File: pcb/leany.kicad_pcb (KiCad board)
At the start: 2 copper layers, 89.4 x 69 mm, 73 parts, among them J1 ST7735S, J2 SWD, J3 USB C, J4 BATT, Q1 AO3401A, Q2 AO3400A, Q3 AO3401A, SW1 ZERO, SW2 HOLD, SW3 RESET, SW4 FLASH, SW5 POWER, U1 STM32F103C8Tx, U2 CH340C, U3 BMI270, U4 BQ25619, U5 AP2112K-3.3, Y1 8MHz

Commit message: refactor: replace the LSM6DSO by a BMI270 (#5)
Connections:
- net /LSM6DSO_CS renamed /BMI270_CS
- net /LSM6DSO_INT1 renamed /BMI270_INT1
- net /LSM6DSO_INT2 renamed /BMI270_INT2
- net /LSM6DSO_SCL renamed /BMI270_SCL
- net /LSM6DSO_SDA renamed /BMI270_SDA
- net /LSM6DSO_SDO renamed /BMI270_SDO

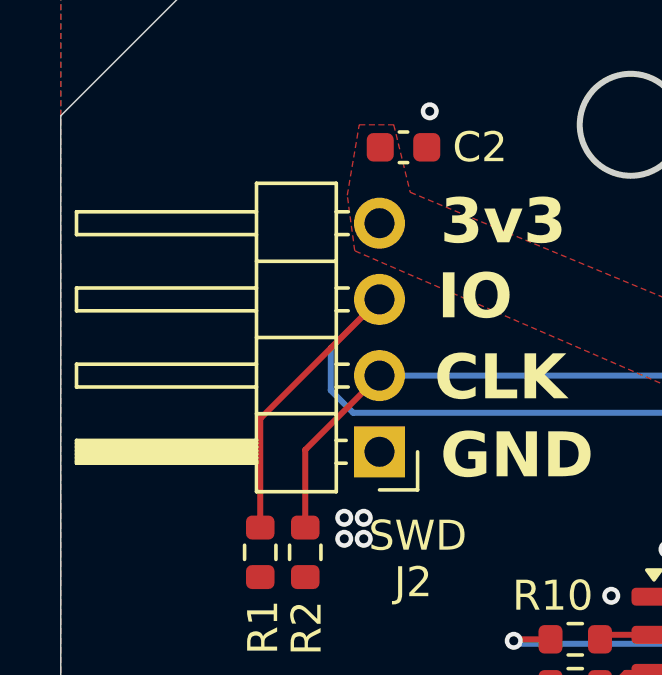
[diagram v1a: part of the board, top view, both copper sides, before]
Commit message: perf: strenghen Mahony filter (#50)
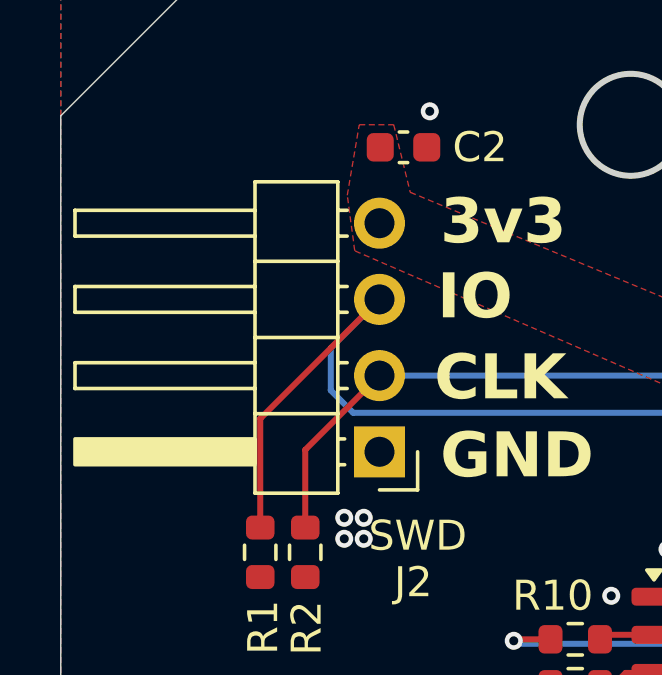
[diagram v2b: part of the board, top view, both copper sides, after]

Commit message: feat: design PCB rev0.3 (#27)
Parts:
- added C25: 100n, leany_footprints:C_0402_1005Metric, F.Cu at (164.9, 103.5)
- added C26: 100n, leany_footprints:C_0402_1005Metric, F.Cu at (149.4, 102.3)
- added C28: 100n, leany_footprints:C_0402_1005Metric, F.Cu at (136.5, 113.2)
- added Q4: AO3401A, Package_TO_SOT_SMD:SOT-23, F.Cu at (130.3, 110.5)
- added Q5: PT8810, Package_TO_SOT_SMD:SOT-23-6, F.Cu at (146.5, 112.6)
- added R25: 100R, leany_footprints:R_0402_1005Metric, F.Cu at (136.5, 111.3)
- added R26: 1k, leany_footprints:R_0402_1005Metric, F.Cu at (142.9, 112.7)
- added REF**: MountingHole_3mm, MountingHole:MountingHole_3mm, F.Cu at (119.6, 121.8)
- added REF**: MountingHole_3mm, MountingHole:MountingHole_3mm, F.Cu at (181.5, 87.0)
- added REF**: MountingHole_3mm, MountingHole:MountingHole_3mm, F.Cu at (181.5, 120.1)
- added TP6: Vin, leany_footprints:TestPoint_Pad_1.0x1.0mm, F.Cu at (137.2, 102.0)
- added TP7: 3.3V, leany_footprints:TestPoint_Pad_1.0x1.0mm, F.Cu at (139.7, 102.0)
- added U6: DW01A, Package_TO_SOT_SMD:SOT-23-6, F.Cu at (139.5, 112.7)
- C10, C12, C14, C17, C2, C20, C21, C22, C23, C3, C4, C5, C6, C7, C8, C9: footprint Capacitor_SMD:C_0603_1608Metric -> leany_footprints:C_0402_1005Metric
- J3: footprint Connector_USB:USB_C_Receptacle_HRO_TYPE-C-31-M-12 -> leany_footprints:USB_C_Receptacle_HRO_TYPE-C-31-M-12
- J4: footprint leany_footprints:wago_2060-452_998-404 -> leany_footprints:wago_2059-302_998-403
- R1, R11, R13, R14, R15, R16, R17, R18, R19, R2, R20, R23, R24, R3, R8: footprint Resistor_SMD:R_0603_1608Metric -> leany_footprints:R_0402_1005Metric
- R10: value 4k7 -> 10k; footprint Resistor_SMD:R_0603_1608Metric -> leany_footprints:R_0402_1005Metric
- R12: value 10k -> 4k7; footprint Resistor_SMD:R_0603_1608Metric -> leany_footprints:R_0402_1005Metric
- R7: value 1M -> 10k; footprint Resistor_SMD:R_0603_1608Metric -> leany_footprints:R_0402_1005Metric
- R9: value 10k -> 1M; footprint Resistor_SMD:R_0603_1608Metric -> leany_footprints:R_0402_1005Metric
- SW1: value ZERO -> SW_HIGH
- SW2: value HOLD -> SW_HIGH
- SW3: value RESET -> SW_LOW; footprint Button_Switch_SMD:SW_Push_1P1T_XKB_TS-1187A -> leany_footprints:SW_Push_1P1T_XKB_TS-1187A
- SW4: value FLASH -> SW_LOW; footprint Button_Switch_SMD:SW_Push_1P1T_XKB_TS-1187A -> leany_footprints:SW_Push_1P1T_XKB_TS-1187A
- TP1: value GND -> DEBUG_OUT
- TP2: value VBUS -> GND
- TP3: value BATT -> VBUS
- TP4: value Vin -> BATT
- TP5: value 3.3V -> +BATT
- U2: value CH340C -> CH340N; footprint Package_SO:SOIC-16_3.9x9.9mm_P1.27mm -> leany_footprints:SOP-8_3.9x4.9mm_P1.27mm
- U3: value BMI270 -> ICM-42688-P
- U5: footprint leany_footprints:TSOT-23-5 -> Package_TO_SOT_SMD:SOT-23-5
- moved TP1 68.7 mm to (163.6, 82.8)
- moved R1 66.3 mm to (168.9, 91.7), turned to 0 degrees
- moved R2 61.7 mm to (165.5, 85.6), turned to 90 degrees
- moved R14 57.6 mm to (127.3, 123.7), turned to 0 degrees
- moved D1 51.6 mm to (149.7, 123.0), turned to 180 degrees
- moved R15 51.4 mm to (127.3, 120.0), turned to 180 degrees
- moved SW4 49.4 mm to (132.1, 121.9), turned to 180 degrees
- moved TP4 49.4 mm to (155.9, 102.3), turned to 180 degrees
- moved R4 47.5 mm to (147.9, 120.3), turned to 90 degrees
- moved R3 47.1 mm to (149.6, 120.4), turned to 90 degrees
- moved R5 46.3 mm to (151.1, 120.2), turned to 90 degrees
- moved R10 45.8 mm to (158.2, 87.1), turned to -90 degrees
- moved SW3 44.9 mm to (141.4, 121.9), turned to 180 degrees
- moved R11 41.2 mm to (154.2, 99.7), turned to 180 degrees
- moved C10 36.4 mm to (154.2, 97.1), turned to 0 degrees
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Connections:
- net /BMI270_INT1 renamed /IMU_INT1
- net /BMI270_INT2 renamed /IMU_INT2
- net /BMI270_SDO renamed /IMU_MISO
- J4 pad 1: +BATT -> Net-(J4-1_1)
- J4 pad 2: +BATT -> Net-(J4-1_1)
- J4 pad 3: GND -> GNDREF
- J4 pad 4: GND -> GNDREF
- R10 pad 1: /FTDI_RX -> +3V3
- R10 pad 2: Net-(U2-TXD) -> Net-(U1-NRST)
- R11 pad 1: /FTDI_TX -> /FTDI_RX
- R11 pad 2: Net-(U2-RXD) -> Net-(U2-TXD)
- R12 pad 1: +3V3 -> /FTDI_TX
- R12 pad 2: /BMI270_SCL -> Net-(U2-RXD)
- R13 pad 2: /BMI270_SDA -> /IMU_CS
- R7 pad 1: Net-(U1-PD0) -> +3V3
- R7 pad 2: Net-(U1-PD1) -> /ST7735S_CS
- R9 pad 1: +3V3 -> Net-(U1-PD0)
- R9 pad 2: Net-(U1-NRST) -> Net-(U1-PD1)
- TP1 pad 1: GND -> /DEBUG_OUT
- TP2 pad 1: Net-(U4-PSEL) -> GND
- TP3 pad 1: BATT_VOLT -> Net-(U4-PSEL)
- TP4 pad 1: SYS -> BATT_VOLT
- TP5 pad 1: +3V3 -> Net-(J4-1_1)
- U1 pad 14: /BMI270_CS -> /IMU_CS
- U1 pad 15: /BMI270_SCL -> /IMU_SCK
- U1 pad 17: /BMI270_SDA -> /IMU_MOSI
- U1 pad 40: unconnected-(U1-PB4-Pad40) -> /DEBUG_OUT
- U2 pad 1: GND -> USB_D+
- U2 pad 2: Net-(U2-TXD) -> USB_D-
- U2 pad 3: Net-(U2-RXD) -> GND
- U2 pad 4: +3V3 -> unconnected-(U2-~{RTS}-Pad4)
- U2 pad 5: USB_D+ -> +3V3
- U2 pad 6: USB_D- -> Net-(U2-TXD)
- U2 pad 7: unconnected-(U2-NC-Pad7) -> Net-(U2-RXD)
- U2 pad 8: unconnected-(U2-NC-Pad8) -> +3V3
- U3 pad 12: /BMI270_CS -> /IMU_CS
- U3 pad 13: /BMI270_SCL -> /IMU_SCK
- U3 pad 14: /BMI270_SDA -> /IMU_MOSI
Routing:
- net +3V3: track 122.6 -> 37.4 mm, vias 2 -> 30
- net GNDREF: track 0.00 -> 43.4 mm
- net /BOOT0: track 18.8 -> 56.3 mm
- net /FTDI_TX: track 50.7 -> 13.8 mm, vias 2 -> 0
- net /FTDI_RX: track 50.3 -> 14.7 mm
- net Net-(U4-PSEL): track 0.00 -> 35.3 mm
- net USB_D+: track 15.4 -> 44.7 mm
- net BATT_EN: track 44.9 -> 17.3 mm
- net Net-(U4-~{QON}): track 11.4 -> 38.9 mm
- net USB_D-: track 18.0 -> 44.4 mm
- net GND: track 0.00 -> 23.1 mm, vias 114 -> 80
- net Net-(U1-NRST): track 29.4 -> 47.0 mm, vias 4 -> 3
- net /BMI270_SDA: track 16.4 -> 0.00 mm, vias 2 -> 0
- net /DEBUG_SWDIO: track 73.2 -> 57.5 mm, vias 1 -> 2
- net /ST7735S_SCL: track 24.7 -> 9.74 mm, vias 0 -> 1
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- added copper zone on In2.Cu, net +3V3
- added copper zone on F.Cu, net BATT_EN
- added copper zone on In1.Cu, net GND
- added copper zone on F.Cu, net Net-(J4-1_1)
- added copper zone on F.Cu, net Net-(Q3-G)
- added copper zone on F.Cu, net Net-(U6-VCC)
- removed copper zone on F.Cu, net /BOOT0
- removed copper zone on F.Cu, net Net-(R14-Pad2)
- removed copper zone on F.Cu, net Net-(U1-NRST)
- removed copper zone on F.Cu, net Net-(U1-PB10)
- removed copper zone on F.Cu, net Net-(U1-PB11)
- removed copper zone on F.Cu, net Net-(U4-BTST)
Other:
- board size 89.4 x 69 mm -> 80.4 x 49.3 mm
- copper layers 2 -> 4
- board text added: "Leany"
- board text added: "rev. 0.3"
- board text removed: "+"
- board text removed: "-"
- board text removed: "3v3"
- board text removed: "BL"
- board text removed: "CLK"
- board text removed: "CS"
- board text removed: "DC"
- board text removed: "GND"
- board text removed: "IO"
- board text removed: "MOSI"
- board text removed: "RST"
- board text removed: "SCL"
- board text removed: "leany rev 0.2"

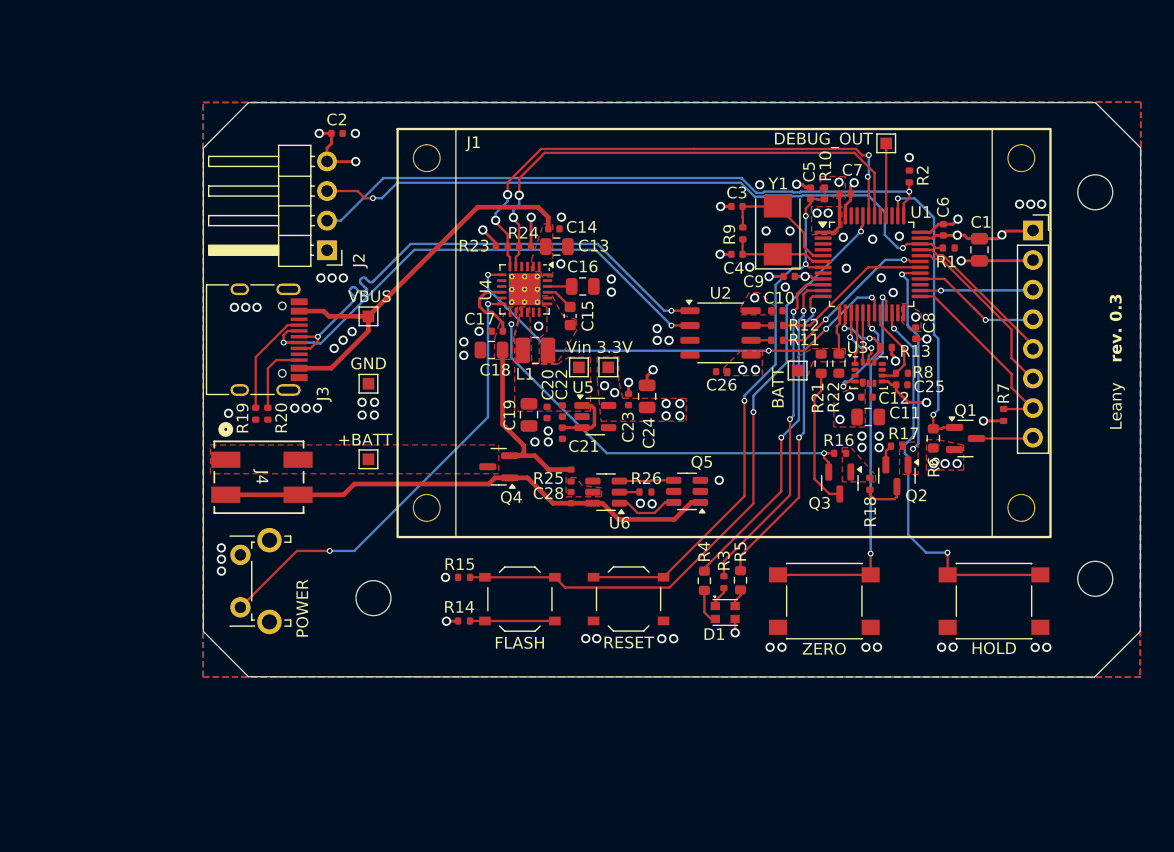
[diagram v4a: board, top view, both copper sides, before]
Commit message: refactor: design PCB rev0.4 and fix validation workflow (#64)
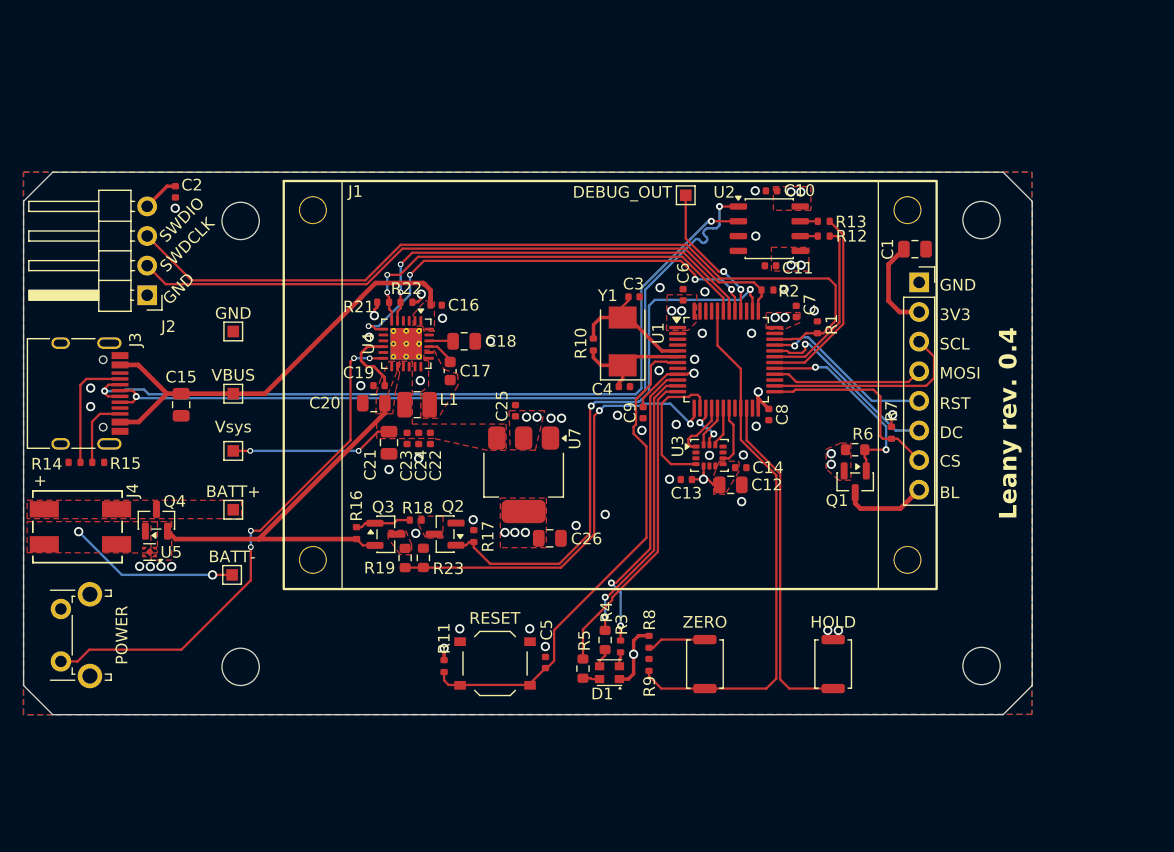
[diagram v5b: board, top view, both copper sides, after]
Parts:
- removed C28: 100n, leany_footprints:C_0402_1005Metric
- removed Q5: PT8810, Package_TO_SOT_SMD:SOT-23-6
- removed R20: 5k1, leany_footprints:R_0402_1005Metric
- removed R24: 4k7, leany_footprints:R_0402_1005Metric
- removed R25: 100R, leany_footprints:R_0402_1005Metric
- removed R26: 1k, leany_footprints:R_0402_1005Metric
- removed REF** (x3): MountingHole_3mm, MountingHole:MountingHole_3mm
- removed SW5: POWER, Button_Switch_THT:SW_Tactile_SPST_Angled_PTS645Vx31-2LFS
- removed TP4: BATT, leany_footprints:TestPoint_Pad_1.0x1.0mm
- removed U6: DW01A, Package_TO_SOT_SMD:SOT-23-6
- added H1: MountingHole, MountingHole:MountingHole_3.2mm_M3, F.Cu at (171.7, 89.3)
- added H2: MountingHole, MountingHole:MountingHole_3.2mm_M3, F.Cu at (171.7, 127.6)
- added H3: MountingHole, MountingHole:MountingHole_3.2mm_M3, F.Cu at (108.2, 89.4)
- added H4: MountingHole, MountingHole:MountingHole_3.2mm_M3, F.Cu at (108.2, 127.7)
- added U7: AMS1117-3.3, Package_TO_SOT_SMD:SOT-223-3_TabPin2, F.Cu at (132.4, 111.2)
- C11, C19: value 10u -> 100n; footprint Capacitor_SMD:C_0805_2012Metric -> leany_footprints:C_0402_1005Metric
- C12, C21, C26: value 100n -> 10u; footprint leany_footprints:C_0402_1005Metric -> Capacitor_SMD:C_0805_2012Metric
- C13: value 22u -> 100n; footprint Capacitor_SMD:C_0805_2012Metric -> leany_footprints:C_0402_1005Metric
- C14, C23: value 1u -> 100n
- C15: value 47n -> 22u; footprint Capacitor_SMD:C_0603_1608Metric -> Capacitor_SMD:C_0805_2012Metric
- C16: value 4.7u -> 1u; footprint Capacitor_SMD:C_0805_2012Metric -> leany_footprints:C_0402_1005Metric
- C17: value 100n -> 47n; footprint leany_footprints:C_0402_1005Metric -> Capacitor_SMD:C_0603_1608Metric
- C18: value 10u -> 4.7u
- C20: value 22n -> 10u; footprint leany_footprints:C_0402_1005Metric -> Capacitor_SMD:C_0805_2012Metric
- C22: value 1u -> 22n
- C24: value 10u -> 1u; footprint Capacitor_SMD:C_0805_2012Metric -> leany_footprints:C_0402_1005Metric
- C25: value 100n -> 1u
- D1: value NH-B2020RGBA-HF -> NH-Z1921RGBA-SG; footprint leany_footprints:NH-B2020RGBA-HF -> leany_footprints:NH-Z1921RGBA-SG
- J4: value BATT -> 2059-302/998-403
- R10: value 10k -> 1M
- R11: value 4k7 -> 10k
- R13: value 10k -> 4k7
- R14: value 10k -> 5k1
- R15: value 100k -> 5k1
- R19: value 5k1 -> 56k; footprint leany_footprints:R_0402_1005Metric -> Resistor_SMD:R_0603_1608Metric
- R21, R22: value 56k -> 4k7; footprint Resistor_SMD:R_0603_1608Metric -> leany_footprints:R_0402_1005Metric
- R23: value 4k7 -> 150k; footprint leany_footprints:R_0402_1005Metric -> Resistor_SMD:R_0603_1608Metric
- R8: value 100k -> 10k
- R9: value 1M -> 100k
- SW1, SW2: footprint leany_footprints:SW_Push_1P1T_NO_6x6mm_H9.5mm -> Button_Switch_SMD:SW_Push_SPST_NO_Alps_SKRK
- SW4: value SW_LOW -> POWER; footprint leany_footprints:SW_Push_1P1T_XKB_TS-1187A -> Button_Switch_THT:SW_Tactile_SPST_Angled_PTS645Vx31-2LFS
- TP5: value +BATT -> BATT+
- TP6: value Vin -> BATT-
- TP7: value 3.3V -> Vsys
- U2: footprint leany_footprints:SOP-8_3.9x4.9mm_P1.27mm -> Package_SO:JEITA_SOIC-8_3.9x4.9mm_P1.27mm
- U5: value AP2112K-3.3 -> AP6683; footprint Package_TO_SOT_SMD:SOT-23-5 -> Package_DFN_QFN:UDFN-4-1EP_1x1mm_P0.65mm_EP0.48x0.48mm
- moved C5 46.2 mm to (134.3, 127.3)
- moved R16 42.0 mm to (118.1, 116.2), turned to -90 degrees
- moved U5 40.0 mm to (100.4, 117.8), turned to 180 degrees
- moved R11 40.0 mm to (125.6, 127.6), turned to -90 degrees
- moved SW4 39.7 mm to (92.8, 127.2), turned to 90 degrees
- moved Q3 39.2 mm to (120.6, 116.3), turned to 0 degrees
- moved Q2 39.1 mm to (125.7, 116.3), turned to 180 degrees
- moved R18 39.1 mm to (123.2, 115.1), turned to 0 degrees
- moved R21 37.9 mm to (120.4, 96.4), turned to 180 degrees
- moved R9 37.9 mm to (143.2, 127.5), turned to 90 degrees
- moved R22 37.5 mm to (122.4, 96.4), turned to 0 degrees
- moved R17 37.1 mm to (128.2, 116.5), turned to 90 degrees
- moved R14 36.1 mm to (93.9, 110.1), turned to 180 degrees
- moved TP6 34.7 mm to (107.4, 119.8), turned to 180 degrees
- moved C15 34.2 mm to (103.1, 105.2), turned to -90 degrees
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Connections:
- net /DEBUG_SWDCLK renamed /DEBUG_SWCLK
- net /IMU_SCK renamed /IMU_SCL
- C13 pad 1: Net-(U4-PSEL) -> +3V3
- C14 pad 1: Net-(U4-PSEL) -> +3V3
- C15 pad 1: Net-(C15-Pad1) -> Net-(U4-PSEL)
- C15 pad 2: Net-(U4-BTST) -> GND
- C16 pad 1: Net-(U4-REGN) -> Net-(U4-PSEL)
- C17 pad 1: +BATT -> Net-(C17-Pad1)
- C17 pad 2: GND -> Net-(U4-BTST)
- C18 pad 1: +BATT -> Net-(U4-REGN)
- C19 pad 1: SYS -> +BATT
- C20 pad 1: SYS -> +BATT
- C21 pad 1: SYS -> Net-(U7-VI)
- C22 pad 1: SYS -> Net-(U7-VI)
- C23 pad 1: +3V3 -> Net-(U7-VI)
- C24 pad 1: +3V3 -> Net-(U7-VI)
- D1 pad 1: Net-(D1-RK) -> +3V3
- D1 pad 2: Net-(D1-BK) -> Net-(D1-RK)
- D1 pad 3: +3V3 -> Net-(D1-GK)
- D1 pad 4: Net-(D1-GK) -> Net-(D1-BK)
- J4 pad 3: GNDREF -> PGND
- J4 pad 4: GNDREF -> PGND
- L1 pad 1: Net-(C15-Pad1) -> Net-(C17-Pad1)
- L1 pad 2: SYS -> Net-(U7-VI)
- Q4 pad 1: GNDREF -> PGND
- R10 pad 1: +3V3 -> Net-(U1-PD0)
- R10 pad 2: Net-(U1-NRST) -> Net-(U1-PD1)
- R11 pad 1: /FTDI_RX -> +3V3
- R11 pad 2: Net-(U2-TXD) -> Net-(U1-NRST)
- R12 pad 1: /FTDI_TX -> /FTDI_RX
- R12 pad 2: Net-(U2-RXD) -> Net-(U2-TXD)
- R13 pad 1: +3V3 -> /FTDI_TX
- R13 pad 2: /IMU_CS -> Net-(U2-RXD)
- R14 pad 1: +3V3 -> Net-(J3-CC1)
- R14 pad 2: Net-(R14-Pad2) -> GND
- R15 pad 1: /BOOT0 -> Net-(J3-CC2)
- R19 pad 1: Net-(J3-CC1) -> BATT_VOLT
- R19 pad 2: GND -> Net-(Q3-D)
- R21 pad 1: BATT_VOLT -> CHG_SDA
- R21 pad 2: Net-(Q3-D) -> +3V3
- R22 pad 1: GND -> CHG_SCL
- R22 pad 2: BATT_VOLT -> +3V3
- R23 pad 1: CHG_SDA -> BATT_VOLT
- R23 pad 2: +3V3 -> GND
- R8 pad 1: GND -> +3V3
- R8 pad 2: /IMU_INT2 -> Net-(R8-Pad2)
- R9 pad 1: Net-(U1-PD0) -> /ZERO_BUTTON
- R9 pad 2: Net-(U1-PD1) -> GND
- SW1 pad 1: Net-(U1-PB10) -> Net-(R8-Pad2)
- SW1 pad 2: GND -> /ZERO_BUTTON
- SW4 pad 1: Net-(R14-Pad2) -> Net-(U4-~{QON})
- SW4 pad 2: /BOOT0 -> GND
- TP6 pad 1: SYS -> PGND
- TP7 pad 1: +3V3 -> Net-(U7-VI)
- U1 pad 14: /IMU_CS -> /IMU_INT1
- U1 pad 18: /IMU_INT1 -> /IMU_CS
- U1 pad 19: CHG_INT -> /IMU_INT2
- U1 pad 20: /IMU_INT2 -> unconnected-(U1-PB2-Pad20)
- U1 pad 21: Net-(U1-PB10) -> /ZERO_BUTTON
- U1 pad 29: BATT_EN -> /ST7735S_BL
- U1 pad 38: /ST7735S_BL -> BATT_EN
- U1 pad 41: unconnected-(U1-PB5-Pad41) -> CHG_INT
- U1 pad 44: /BOOT0 -> /ZERO_BUTTON
- U4 pad 15: SYS -> Net-(U7-VI)
- U4 pad 16: SYS -> Net-(U7-VI)
- U4 pad 19: Net-(C15-Pad1) -> Net-(C17-Pad1)
- U4 pad 20: Net-(C15-Pad1) -> Net-(C17-Pad1)
- U5 pad 1: SYS -> +BATT
- U5 pad 2: GND -> PGND
- U5 pad 3: SYS -> PGND
- U5 pad 4: unconnected-(U5-NC-Pad4) -> GND
- U5 pad 5: +3V3 -> GND
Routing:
- net /BOOT0: track 56.3 -> 0.00 mm, vias 2 -> 0
- net /ZERO_BUTTON: track 0.00 -> 45.8 mm
- net GNDREF: track 43.4 -> 0.00 mm
- net BATT_VOLT: track 3.70 -> 38.5 mm, vias 0 -> 2
- net Net-(U1-PB10): track 33.6 -> 0.00 mm, vias 2 -> 0
- net BATT_EN: track 17.3 -> 48.8 mm
- net USB_D-: track 44.4 -> 69.1 mm
- net USB_D+: track 44.7 -> 69.2 mm
- net GND: track 23.1 -> 0.00 mm, vias 80 -> 43
- net +BATT: track 58.5 -> 40.5 mm, vias 2 -> 0
- net /DEBUG_SWDIO: track 57.5 -> 72.3 mm, vias 2 -> 0
- net PGND: track 0.00 -> 14.7 mm, vias 0 -> 2
- net Net-(U7-VI): track 0.00 -> 14.1 mm, vias 0 -> 2
- net Net-(Q3-D): track 12.0 -> 0.00 mm
- net CHG_SDA: track 45.8 -> 36.2 mm, vias 4 -> 2
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- added copper zone on F.Cu, net Net-(C17-Pad1)
- added copper zone on F.Cu, net Net-(Q2-D)
- added copper zone on F.Cu, net Net-(Q3-D)
- added copper zone on F.Cu, net Net-(U7-VI)
- added copper zone on F.Cu, net PGND
- removed copper zone on F.Cu, net BATT_EN
- removed copper zone on F.Cu, net BATT_VOLT
- removed copper zone on F.Cu, net Net-(C15-Pad1)
- removed copper zone on F.Cu, net Net-(Q3-G)
- removed copper zone on F.Cu, net Net-(U6-VCC)
- removed copper zone on F.Cu, net SYS
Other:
- board size 80.4 x 49.3 mm -> 86.5 x 46.5 mm
- board text added: "0.14"
- board text added: "0.34"
- board text added: "22"
- board text added: "26"
- board text added: "3V3"
- board text added: "4mm"
- board text added: "5.5mm"
- board text added: "BL"
- board text added: "CS"
- board text added: "DC"
- board text added: "GND"
- board text added: "Leany rev. ${REVISION}"
- board text added: "MOSI"
- board text added: "RST"
- board text added: "SCL"
- board text added: "SWDCLK"
- board text added: "SWDIO"
- board text added: "TP6"
- board text removed: "0.2"
- board text removed: "0.75"
- board text removed: "18"
- board text removed: "24"
- board text removed: "7mm"
- board text removed: "9mm"
- board text removed: "Leany"
- board text removed: "rev. 0.3"
